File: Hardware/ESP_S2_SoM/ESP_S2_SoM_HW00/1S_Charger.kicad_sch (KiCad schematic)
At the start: 14 parts, among them U201 BQ24075RGTR

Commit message: lots of work on routing
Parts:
- removed TP201: TestPoint, TestPoint:TestPoint_Pad_D1.0mm, symbol Connector:TestPoint
- added R1: R, Resistor_SMD:R_0402_1005Metric, symbol Component_lib:R
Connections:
- net GND: now also R1.1, R1.2

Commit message: led footprint update
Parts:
- D201, D202: footprint Component_lib:LED_0402_1005Metric_DUALSIDE -> LED_SMD:LED_0402_1005Metric
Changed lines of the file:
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@@
       (effects (font (size 1.27 1.27)) (justify right))
     )
-    (property "Footprint" "Component_lib:LED_0402_1005Metric_DUALSIDE" (at 213.36 95.25 0)
+    (property "Footprint" "LED_SMD:LED_0402_1005Metric" (at 213.36 95.25 0)
       (effects (font (size 1.27 1.27)) hide)
     )
@@
       (effects (font (size 1.27 1.27)) (justify right))
     )
-    (property "Footprint" "Component_lib:LED_0402_1005Metric_DUALSIDE" (at 223.52 95.25 0)
-      (effects (font (size 1.27 1.27)) hide)
-    )
+    (property "Footprint" "LED_SMD:LED_0402_1005Metric" (at 223.52 95.25 0)
+      (effects (font (size 1.27 1.27)) hide)
+    )

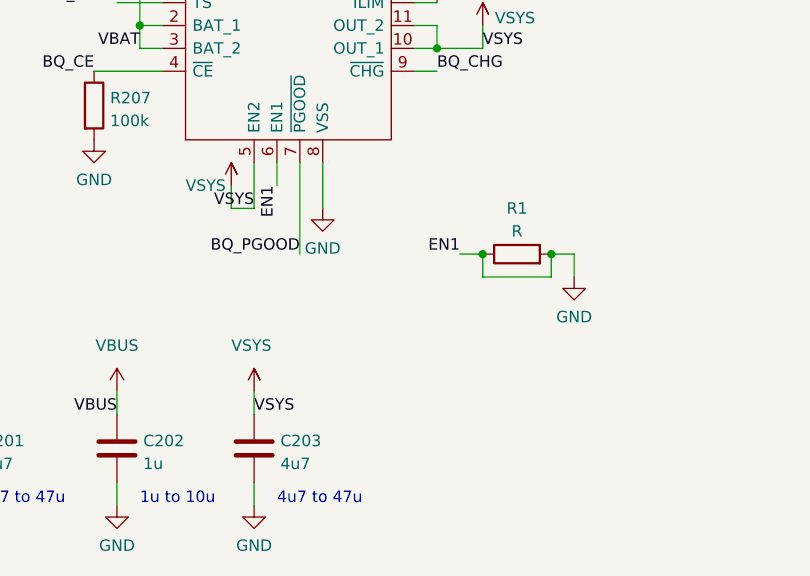
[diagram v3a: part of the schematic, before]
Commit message: Routing ESP32S2
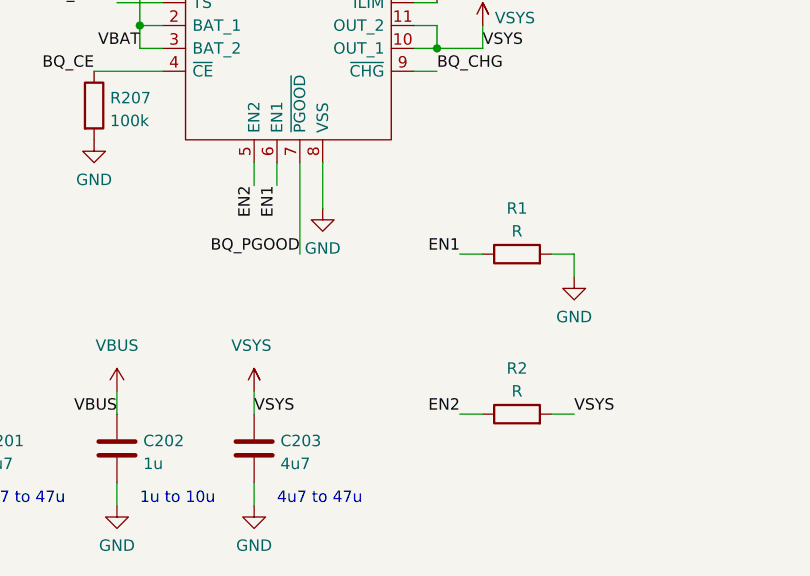
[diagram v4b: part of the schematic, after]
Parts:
- added R2: R, Resistor_SMD:R_0402_1005Metric, symbol Component_lib:R
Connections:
- net GND: no longer R1.1, U201.6 (EN1)
- net VSYS: now also R2.2; no longer U201.5 (EN2)
- new net EN1: R1.1, U201.6 (EN1)
- new net EN2: R2.1, U201.5 (EN2)
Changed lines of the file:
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@@
   (junction (at 218.44 78.74) (diameter 0) (color 0 0 0 0)
   )
-  (junction (at 132.08 114.3) (diameter 0) (color 0 0 0 0)
-  )
   (junction (at 93.98 88.9) (diameter 0) (color 0 0 0 0)
   )
-  (junction (at 139.7 114.3) (diameter 0) (color 0 0 0 0)
-  )
   (junction (at 127 91.44) (diameter 0) (color 0 0 0 0)
   )
-  (wire (pts (xy 139.7 116.84) (xy 139.7 114.3))
-    (stroke (width 0) (type default))
-  )
   (wire (pts (xy 266.7 43.18) (xy 269.24 43.18))
     (stroke (width 0) (type default))
   )
-  (wire (pts (xy 132.08 114.3) (xy 132.08 116.84))
-    (stroke (width 0) (type default))
-  )
   (wire (pts (xy 104.14 71.12) (xy 104.14 76.2))
     (stroke (width 0) (type default))
   )
-  (wire (pts (xy 104.14 109.22) (xy 104.14 106.68))
-    (stroke (width 0) (type default))
-  )
   (wire (pts (xy 106.68 129.54) (xy 106.68 132.08))
     (stroke (width 0) (type default))
   )
-  (wire (pts (xy 132.08 116.84) (xy 139.7 116.84))
-    (stroke (width 0) (type default))
-  )
   (wire (pts (xy 124.46 88.9) (xy 127 88.9))
     (stroke (width 0) (type default))
@@
     (stroke (width 0) (type default))
   )
+  (wire (pts (xy 129.54 132.08) (xy 132.08 132.08))
+    (stroke (width 0) (type default))
+  )
   (wire (pts (xy 218.44 78.74) (xy 223.52 78.74))
     (stroke (width 0) (type default))
@@
     (stroke (width 0) (type default))
   )
+  (wire (pts (xy 139.7 132.08) (xy 142.24 132.08))
+    (stroke (width 0) (type default))
+  )
   (wire (pts (xy 124.46 91.44) (xy 127 91.44))
     (stroke (width 0) (type default))
@@
     (stroke (width 0) (type default))
   )
-  (wire (pts (xy 106.68 109.22) (xy 106.68 104.14))
-    (stroke (width 0) (type default))
-  )
   (wire (pts (xy 223.52 78.74) (xy 223.52 81.28))
     (stroke (width 0) (type default))
@@
     (stroke (width 0) (type default))
   )
-  (wire (pts (xy 104.14 109.22) (xy 106.68 109.22))
-    (stroke (width 0) (type default))
-  )
   (wire (pts (xy 109.22 104.14) (xy 109.22 106.68))
     (stroke (width 0) (type default))
@@
   )
   (wire (pts (xy 269.24 22.86) (xy 266.7 22.86))
+    (stroke (width 0) (type default))
+  )
+  (wire (pts (xy 106.68 104.14) (xy 106.68 106.68))
     (stroke (width 0) (type default))
   )
@@
     (effects (font (size 1.27 1.27)) (justify right bottom))
   )
+  (label "VSYS" (at 142.24 132.08 0) (fields_autoplaced)
+    (effects (font (size 1.27 1.27)) (justify left bottom))
+  )
   (label "BQ_CHG" (at 127 93.98 0) (fields_autoplaced)
     (effects (font (size 1.27 1.27)) (justify left bottom))
   )
+  (label "EN2" (at 129.54 132.08 180) (fields_autoplaced)
+    (effects (font (size 1.27 1.27)) (justify right bottom))
+  )
   (label "VBAT" (at 266.7 38.1 180) (fields_autoplaced)
     (effects (font (size 1.27 1.27)) (justify right bottom))
@@
     (effects (font (size 1.27 1.27)) (justify right bottom))
   )
+  (label "EN2" (at 106.68 106.68 270) (fields_autoplaced)
+    (effects (font (size 1.27 1.27)) (justify right bottom))
+  )
   (label "BQ_CE" (at 88.9 93.98 180) (fields_autoplaced)
     (effects (font (size 1.27 1.27)) (justify right bottom))
@@
   (label "ISET" (at 106.68 76.2 90) (fields_autoplaced)
     (effects (font (size 1.27 1.27)) (justify left bottom))
-  )
-  (label "VSYS" (at 106.68 109.22 180) (fields_autoplaced)
-    (effects (font (size 1.27 1.27)) (justify right bottom))
   )
   (label "SYSOFF" (at 109.22 76.2 90) (fields_autoplaced)
@@
         (path "/c3b08055-08a5-4979-9bf8-f36ab0917722/2d6b4425-2527-49bd-b090-a8cc21f6a212"
           (reference "#VBAT0201") (unit 1)
+        )
+      )
+    )
+  )
+  (symbol (lib_id "Component_lib:R") (at 132.08 132.08 90) (unit 1)
+    (in_bom yes) (on_board yes) (dnp no) (fields_autoplaced)
+    (property "Reference" "R2" (at 135.89 127 90)
+      (effects (font (size 1.27 1.27)))
+    )
+    (property "Value" "R" (at 135.89 129.54 90)
+      (effects (font (size 1.27 1.27)))
+    )
+    (property "Footprint" "Resistor_SMD:R_0402_1005Metric" (at 135.89 133.858 90)
+      (effects (font (size 1.27 1.27)) hide)
+    )
+    (property "Datasheet" "~" (at 135.89 132.08 0)
+      (effects (font (size 1.27 1.27)) hide)
+    )
+    (pin "1")
+    (pin "2")
+    (instances
+      (project "ESP_S2_SoM_HW00"
+        (path "/14b8af2e-80ef-48c8-890f-5f81b4faa854/a8f40f14-1954-4df1-a27b-4ef4decd9fbc"
+          (reference "R2") (unit 1)
         )
       )
@@
         )
       )
-    )
-  )
-  (symbol (lib_id "Component lib:VSYS") (at 104.14 106.68 0) (unit 1)
-    (in_bom no) (on_board no) (dnp no)
-    (property "Reference" "#VSYS0106" (at 109.22 101.6 0)
-      (effects (font (size 1.27 1.27)) hide)
-    )
-    (property "Value" "VSYS" (at 99.06 106.68 0)
-      (effects (font (size 1.27 1.27)) (justify left))
-    )
-    (property "Footprint" "" (at 104.14 106.68 0)
-      (effects (font (size 1.27 1.27)) hide)
-    )
-    (property "Datasheet" "" (at 104.14 106.68 0)
-      (effects (font (size 1.27 1.27)) hide)
-    )
-    (pin "")
-    (instances
-      (project "ESP_S2_SoM_HW00"
-        (path "/14b8af2e-80ef-48c8-890f-5f81b4faa854/a8f40f14-1954-4df1-a27b-4ef4decd9fbc"
-          (reference "#VSYS0106") (unit 1)
-        )
-      )
-      (project "PMK_Keyboard"
-        (path "/c3b08055-08a5-4979-9bf8-f36ab0917722/2d6b4425-2527-49bd-b090-a8cc21f6a212"
-          (reference "#VSYS0106") (unit 1)
-        )
-      )

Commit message: Small cartouche mistake
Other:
- title: PSoM - ESP S3 -> PSoM - ESP S2
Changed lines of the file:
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@@
   (paper "A4")
   (title_block
-    (title "PSoM - ESP S3")
+    (title "PSoM - ESP S2")
     (date "2023-04-17")
     (rev "HW00")
